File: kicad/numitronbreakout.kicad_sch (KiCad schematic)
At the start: 12 parts, among them J1 Conn_01x06, U1 HV5812WG-G, U2 LM317_TO-220, U3 LM317_TO-220, U4 IV-12, U5 IV-12

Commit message: updated pin connector, layout
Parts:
- J1: footprint Connector_PinHeader_2.54mm:PinHeader_1x08_P2.54mm_Horizontal -> NewFootprints:66100811722; Manufacturer_Name (none) -> Würth Elektronik; Manufacturer_Part_Number (none) -> 66100811722
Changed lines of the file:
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@@
 			)
 		)
-		(property "Footprint" "Connector_PinHeader_2.54mm:PinHeader_1x08_P2.54mm_Horizontal"
+		(property "Footprint" "NewFootprints:66100811722"
 			(at 25.4 36.83 0)
 			(effects
@@
 			)
 		)
-		(property "Datasheet" "~"
+		(property "Datasheet" "https://www.we-online.com/katalog/datasheet/66100211722.pdf"
 			(at 25.4 36.83 0)
 			(effects
@@
 			)
 		)
-		(property "Description" "Generic connector, single row, 01x08, script generated (kicad-library-utils/schlib/autogen/connector/)"
+		(property "Description" "CONN HEADER R/A 8POS 2.54MM"
 			(at 25.4 36.83 0)
 			(effects
@@
 			(at 25.4 36.83 0)
 			(effects
+				(font
+					(size 1.27 1.27)
+				)
+				(hide yes)
+			)
+		)
+		(property "Manufacturer_Name" "Würth Elektronik"
+			(at 25.4 36.83 0)
+			(effects
+				(font
+					(size 1.27 1.27)
+				)
+				(hide yes)
+			)
+		)
+		(property "Manufacturer_Part_Number" "66100811722"
+			(at 25.4 36.83 0)
+			(effects

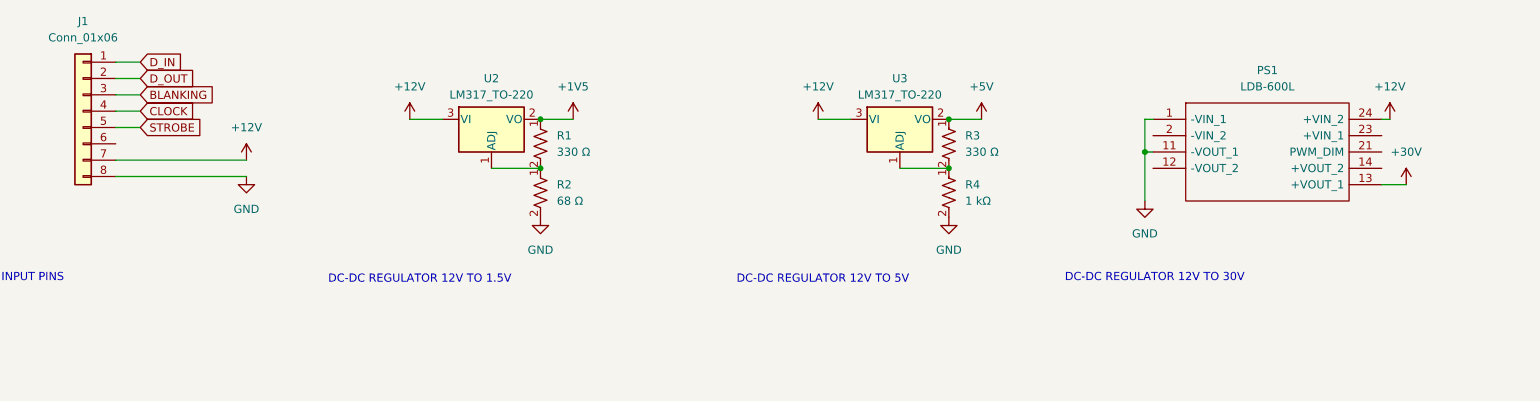
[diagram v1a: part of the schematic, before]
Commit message: updated boost converter and added dimming capability
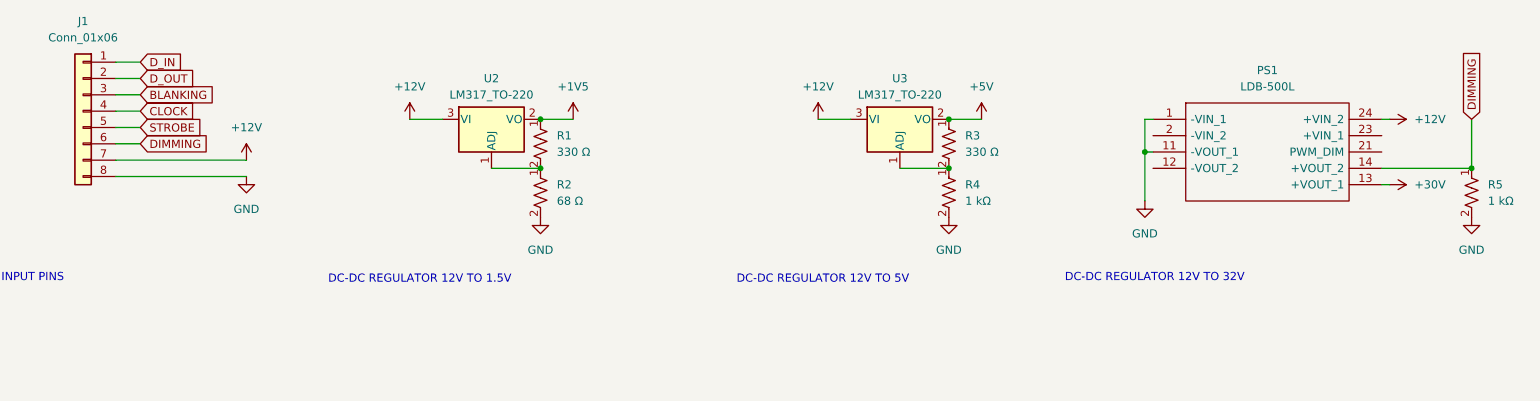
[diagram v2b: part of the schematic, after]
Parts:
- added R5: 1 kΩ, Resistor_SMD:R_1206_3216Metric_Pad1.30x1.75mm_HandSolder, symbol Device:R_US
- PS1: value LDB-600L -> LDB-500L; Description_1 LED Power Supplies 9-28Vin 2-30Vout 600mA pin style -> 500mA 2 ~ 32V Constant Current LED Driver Buck-Boost Topolo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; Height 12.25 -> (none); Manufacturer_Name MEAN WELL USA Inc. -> (none); Manufacturer_Part_Number LDB-600L -> (none); Mouser Part Number 709-LDB-600L -> (none); Mouser Price/Stock https://www.mouser.co.uk/ProductDetail/MEAN-WELL/LDB-600L/?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 -> (none); Part No LDB-600L -> LDB-500L
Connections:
- net GND: now also R5.2
- net DIMMING: now reaches J1.6 (Pin_6)
- net DIMMING: now also PS1.14 (+VOUT_2), R5.1
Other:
- note added: "DC-DC REGULATOR 12V TO 32V"
- note removed: "DC-DC REGULATOR 12V TO 30V"
